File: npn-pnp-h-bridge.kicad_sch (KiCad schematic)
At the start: 44 parts, among them J1 S4B-PH-K-S_LF__SN_, J2 S2B-PH-K-S_LF__SN_, Q1 MMBT3904, Q2 MMBT3904, Q3 MMBT3904, Q4 MMBT3904

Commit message: Use handsoldering-footprints for diodes
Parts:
- D1, D2, D3, D4: footprint Diode_SMD:D_SMA -> Diode_SMD:D_SMA_Handsoldering
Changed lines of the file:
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@@
 			)
 		)
-		(property "Footprint" "Diode_SMD:D_SMA"
+		(property "Footprint" "Diode_SMD:D_SMA_Handsoldering"
 			(at 97.155 127 0)
 			(effects
@@
 			)
 		)
-		(property "Footprint" "Diode_SMD:D_SMA"
+		(property "Footprint" "Diode_SMD:D_SMA_Handsoldering"
 			(at 81.915 127 0)
 			(effects
@@
 			)
 		)
-		(property "Footprint" "Diode_SMD:D_SMA"
+		(property "Footprint" "Diode_SMD:D_SMA_Handsoldering"
 			(at 97.155 83.82 0)
 			(effects
@@
 			)
 		)
-		(property "Footprint" "Diode_SMD:D_SMA"
+		(property "Footprint" "Diode_SMD:D_SMA_Handsoldering"
 			(at 81.915 83.82 0)
 			(effects

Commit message: beautify schematic
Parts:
- removed V4: 5, symbol Simulation_SPICE:VDC
- removed V5: 0, symbol Simulation_SPICE:VDC
- removed V8: 3.3, symbol Simulation_SPICE:VDC
- R13, R14: value 180 -> 100
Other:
- moved on the sheet: C1, C2, C3, C4, C5, D1, D2, D3, D4, D5, D6, D99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

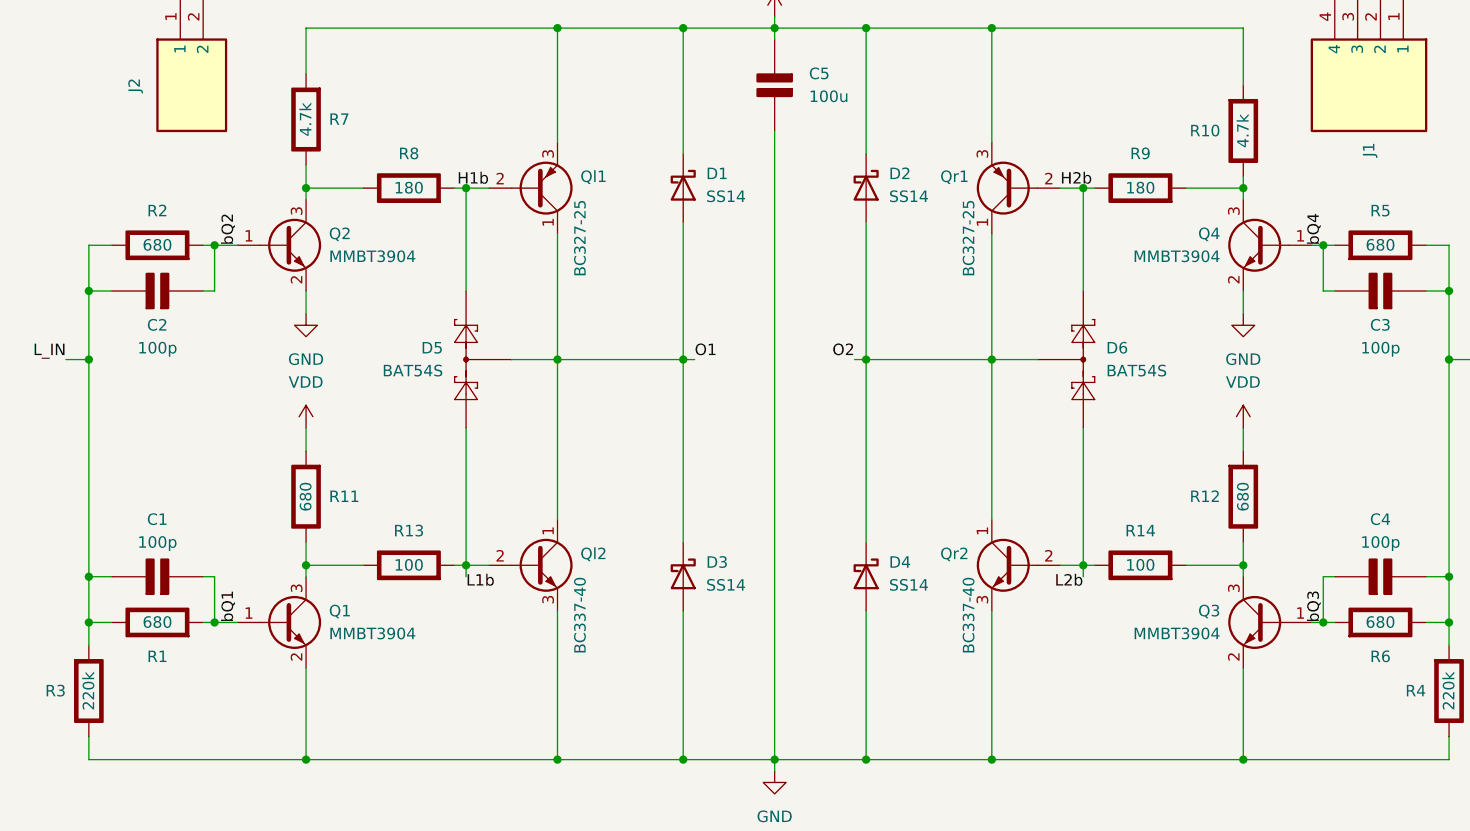
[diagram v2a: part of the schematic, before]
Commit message: Changed MMBT3904 for a dual-NPN MMDT3904 for miniturization
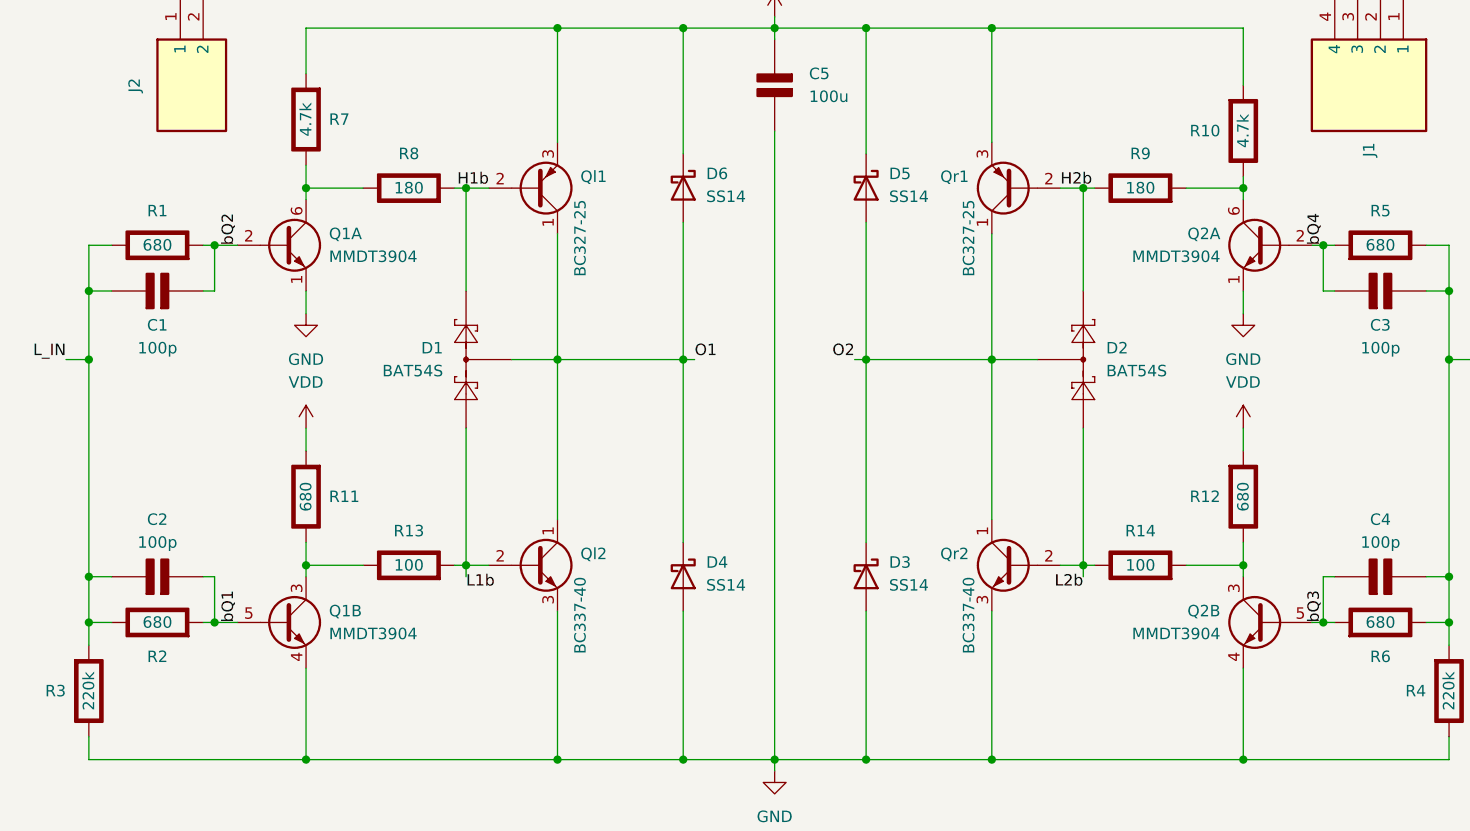
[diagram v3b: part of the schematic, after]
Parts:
- removed Q1, Q2, Q3, Q4: MMBT3904, Package_TO_SOT_SMD:SOT-23_Handsoldering, symbol Transistor_BJT:MMBT3904
- added Q1, Q2: MMDT3904, Package_TO_SOT_SMD:SOT-363_SC-70-6_Handsoldering, symbol Transistor_BJT:MMDT3904
- renumbered C2 to C1, C1 to C2, D5 to D1, D6 to D2, D4 to D3, D3 to D4, D2 to D5, D1 to D6, R2 to R1, R1 to R2
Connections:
- net GND: now also Q1.1 (E1), Q1.4 (E2), Q2.1 (E1), Q2.4 (E2)
- net bQ1: now also Q1.5 (B2)
- net bQ2: now also Q1.2 (B1)
- net bQ3: now also Q2.5 (B2)
- net bQ4: now also Q2.2 (B1)
- net at R7.1 (+), R8.1 (+): now also Q1.6 (C1)
- net at R12.1 (+), R14.2 (-): now also Q2.3 (C2)
- net at R10.1 (+), R9.2 (-): now also Q2.6 (C1)
- net at R11.1 (+), R13.1 (+): now also Q1.3 (C2)

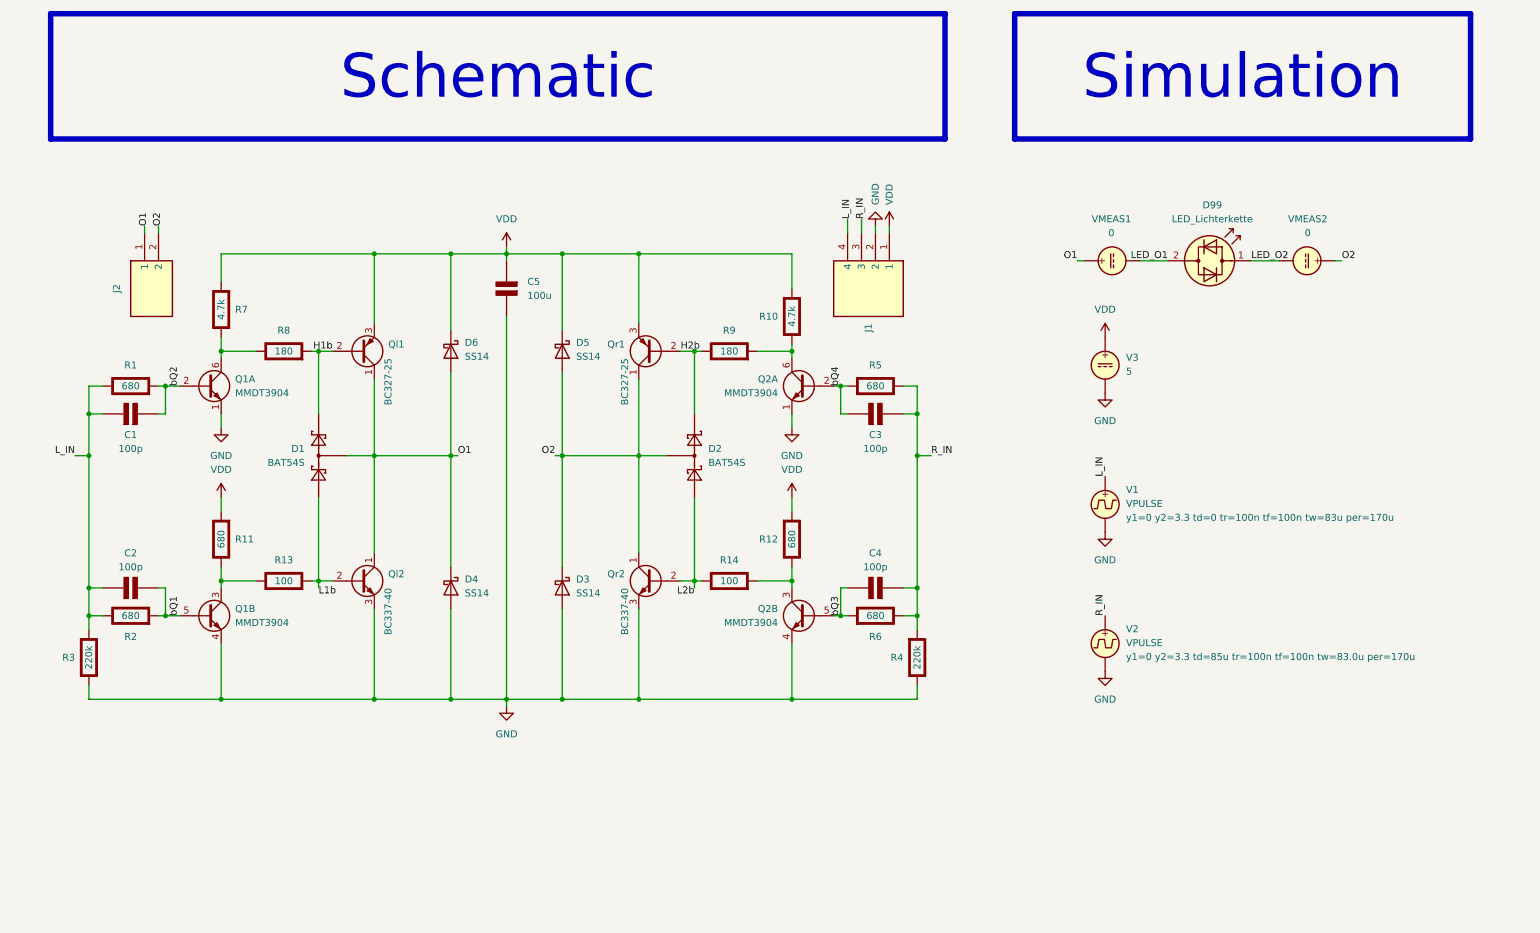
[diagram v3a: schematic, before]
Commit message: final touches for dual-npn-package
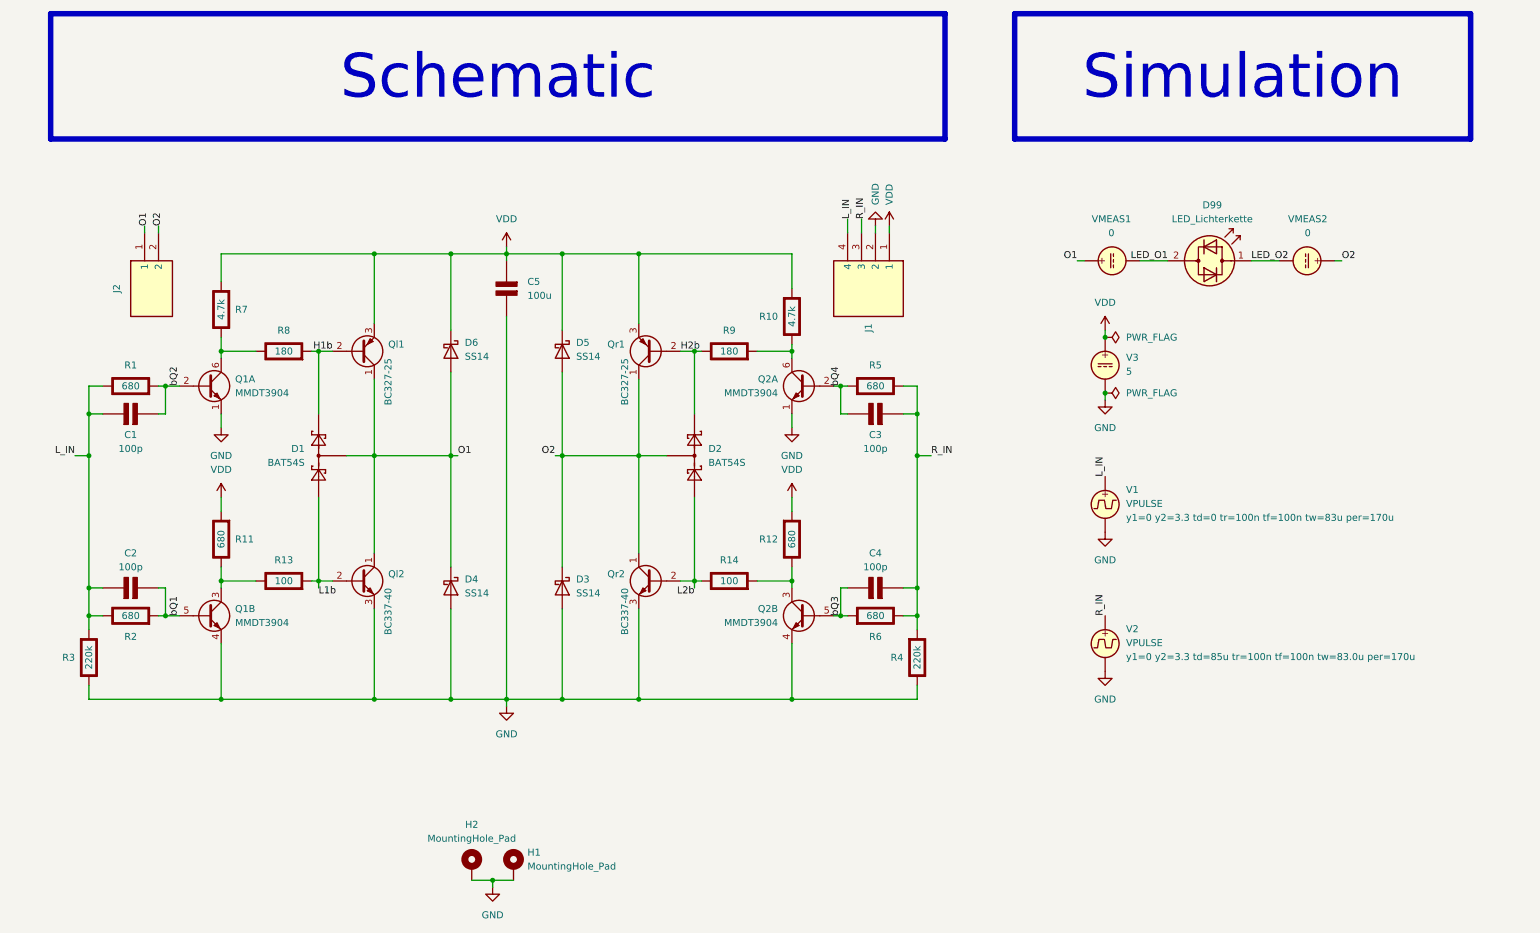
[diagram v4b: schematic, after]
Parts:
- added H1, H2: MountingHole_Pad, MountingHole:MountingHole_2.2mm_M2_Pad_TopBottom, symbol Mechanical:MountingHole_Pad
- J1: footprint Misc:CONN_S4B-PH-K-S_JST -> Misc:JST_PH_S4B-PH-K_1x04_P2.00mm_Horizontal
- J2: footprint Misc:DS2BPHKSLFSN -> Misc:JST_PH_S2B-PH-K_1x02_P2.00mm_Horizontal
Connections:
- net GND: now also H1.1, H2.1

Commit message: pushed out the connectors to match the case
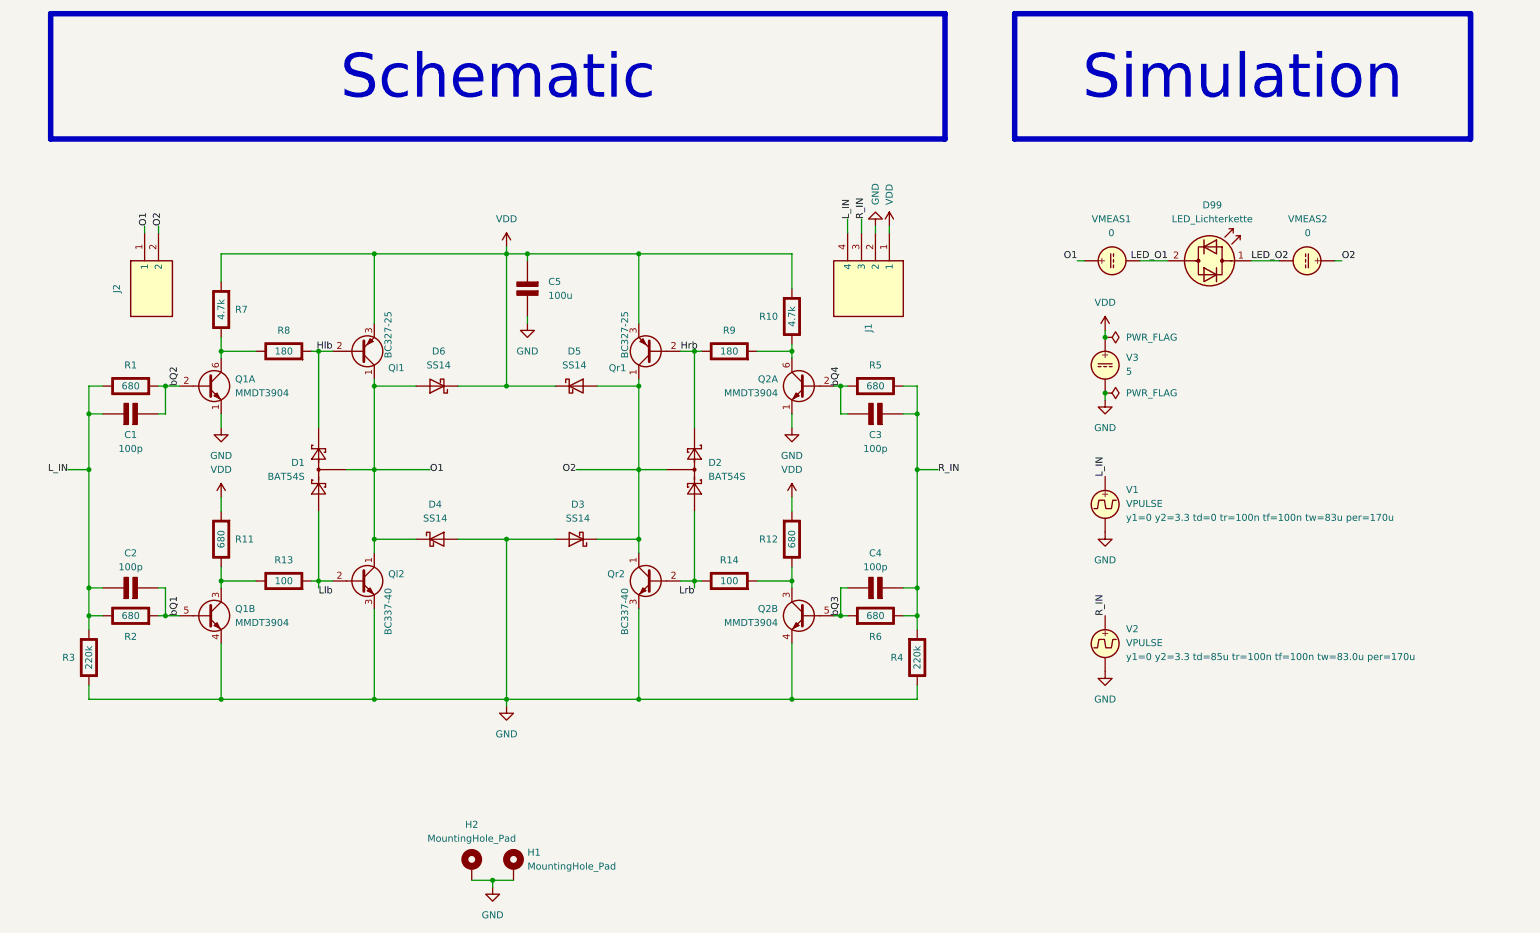
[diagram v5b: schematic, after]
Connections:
- net H1b renamed Hlb
- net H2b renamed Hrb
- net L1b renamed Llb
- net L2b renamed Lrb
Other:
- moved on the sheet: C5, D1, D2, D3, D4, D5, D6
